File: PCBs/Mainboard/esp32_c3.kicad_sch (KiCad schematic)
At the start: 21 parts, among them U1 ESP32-C3, Y1 40MHz

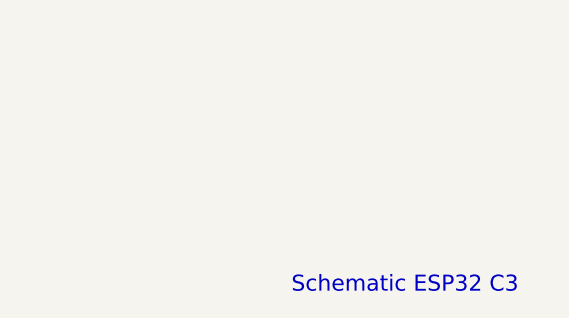
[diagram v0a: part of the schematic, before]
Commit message: Add progress report for 31.1.2025 Update relevant source files
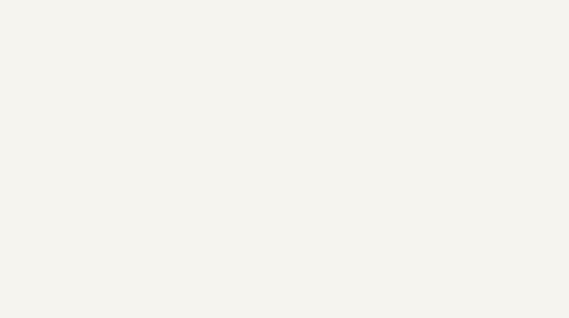
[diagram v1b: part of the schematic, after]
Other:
- note removed: "Schematic ESP32 C3"
- title: (none) -> ESP32 C3
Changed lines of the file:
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@@
 	(generator_version "8.0")
 	(paper "A4")
+	(title_block
+		(title "ESP32 C3")
+	)
 	(junction
 		(at 127 41.91)
@@
 		)
 	)
-	(text "Schematic ESP32 C3"
-		(exclude_from_sim no)
-		(at 200.66 189.992 0)
-		(effects
-			(font
-				(size 1.778 1.778)
-			)
-		)
-	)
 	(text "Strapping Pins\n"
 		(exclude_from_sim no)
@@
 	(label "RF_ANTENNA"
 		(at 170.18 55.88 0)
-		(fields_autoplaced yes)
 		(effects
 			(font
@@
 	(label "RF_ANTENNA"
 		(at 100.33 74.93 0)
-		(fields_autoplaced yes)
 		(effects
 			(font
@@
 		(shape input)
 		(at 113.03 85.09 180)
-		(fields_autoplaced yes)
 		(effects
 			(font
@@
 		(shape input)
 		(at 110.49 107.95 180)
-		(fields_autoplaced yes)
 		(effects
 			(font
@@
 		(shape input)
 		(at 110.49 105.41 180)
-		(fields_autoplaced yes)
 		(effects
 			(font
@@
 		(shape input)
 		(at 171.45 102.87 0)
-		(fields_autoplaced yes)
 		(effects
 			(font
@@
 		(shape input)
 		(at 171.45 82.55 0)
-		(fields_autoplaced yes)
 		(effects
 			(font
@@
 		(shape input)
 		(at 201.93 107.95 0)
-		(fields_autoplaced yes)
 		(effects
 			(font
@@
 		(shape input)
 		(at 171.45 85.09 0)
-		(fields_autoplaced yes)
 		(effects
 			(font
@@
 		(shape input)
 		(at 110.49 102.87 180)
-		(fields_autoplaced yes)
 		(effects
 			(font
@@
 		(shape input)
 		(at 171.45 100.33 0)
-		(fields_autoplaced yes)
 		(effects
 			(font
@@
 		(shape input)
 		(at 113.03 87.63 180)
-		(fields_autoplaced yes)
 		(effects
 			(font
@@
 		(shape input)
 		(at 110.49 100.33 180)
-		(fields_autoplaced yes)
 		(effects
 			(font
@@
 		(shape input)
 		(at 180.34 74.93 0)
-		(fields_autoplaced yes)
 		(effects
 			(font
@@
 		(shape input)
 		(at 182.88 100.33 0)
-		(fields_autoplaced yes)
 		(effects
 			(font
@@
 		(shape input)
 		(at 170.18 110.49 0)
-		(fields_autoplaced yes)
 		(effects
 			(font
@@
 		(shape input)
 		(at 180.34 77.47 0)
-		(fields_autoplaced yes)
-		(effects
-			(font
+		(effects
+			(font
